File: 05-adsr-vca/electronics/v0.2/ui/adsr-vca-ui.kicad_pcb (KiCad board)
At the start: 2 copper layers, 58 x 110 mm, 31 parts, among them J1 Conn_02x03_Odd_Even, J3 Conn_02x03_Odd_Even, J4 Conn_01x02, J5 Conn_01x06, J6 Conn_02x03_Odd_Even, J8 Conn_02x03_Odd_Even

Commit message: Redraw ADSR PCBs to be on top half of the UI
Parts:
- moved J5 104.5 mm to (143.0, 47.0)
- moved G*** 66.3 mm to (211.4, 50.5)
- moved J3 57.5 mm to (155.5, 91.5), turned to 180 degrees
- moved G*** 56.4 mm to (204.6, 81.1)
- moved J6 45.5 mm to (133.5, 49.5), turned to -90 degrees
- moved D1 17.3 mm to (173.0, 45.7), turned to -90 degrees
- moved J4 16.0 mm to (178.7, 81.6)
- moved H5 13.4 mm to (127.3, 105.7)
- moved H6 13.4 mm to (178.7, 105.7)
- moved J1 7.02 mm to (151.5, 101.0), turned to 90 degrees
- moved J8 6.52 mm to (128.5, 93.5)
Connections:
- J8 pad 2: DECAY_1 -> ATTACK_3
- J8 pad 3: ENV_OUT -> RELEASE_1
- J8 pad 4: ATTACK_3 -> ENV_OUT
- J8 pad 5: unconnected-(J8-Pin_5-Pad5) -> DECAY_1
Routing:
- net VCA_OUT: track 9.75 -> 109.3 mm
- net VCA_IN_DEFAULT: track 19.0 -> 112.5 mm, vias 0 -> 2
- net VCA_CV: track 9.36 -> 88.1 mm
- net VCA_CV_DEFAULT: track 48.0 -> 120.6 mm, vias 2 -> 0
- net SUSTAIN_3: track 104.2 -> 33.9 mm
- net SUSTAIN_1: track 37.0 -> 98.4 mm, vias 0 -> 2
- net SUSTAIN_2: track 37.7 -> 97.7 mm, vias 0 -> 2
- net VCA_OUT_DEFAULT: track 53.9 -> 110.4 mm
- net DECAY_1: track 100.5 -> 65.9 mm, vias 0 -> 1
- net ENV_OUT: track 86.2 -> 59.2 mm, vias 0 -> 2
- net GATE_DEFAULT: track 49.7 -> 73.1 mm, vias 0 -> 4
- net RELEASE_1: track 2.50 -> 19.4 mm, vias 0 -> 1
- net LED_K: track 65.0 -> 48.7 mm, vias 0 -> 2
- net ENV_OUT_DEFAULT: track 65.3 -> 80.4 mm
- net A1_D3_R3: track 65.3 -> 78.9 mm
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
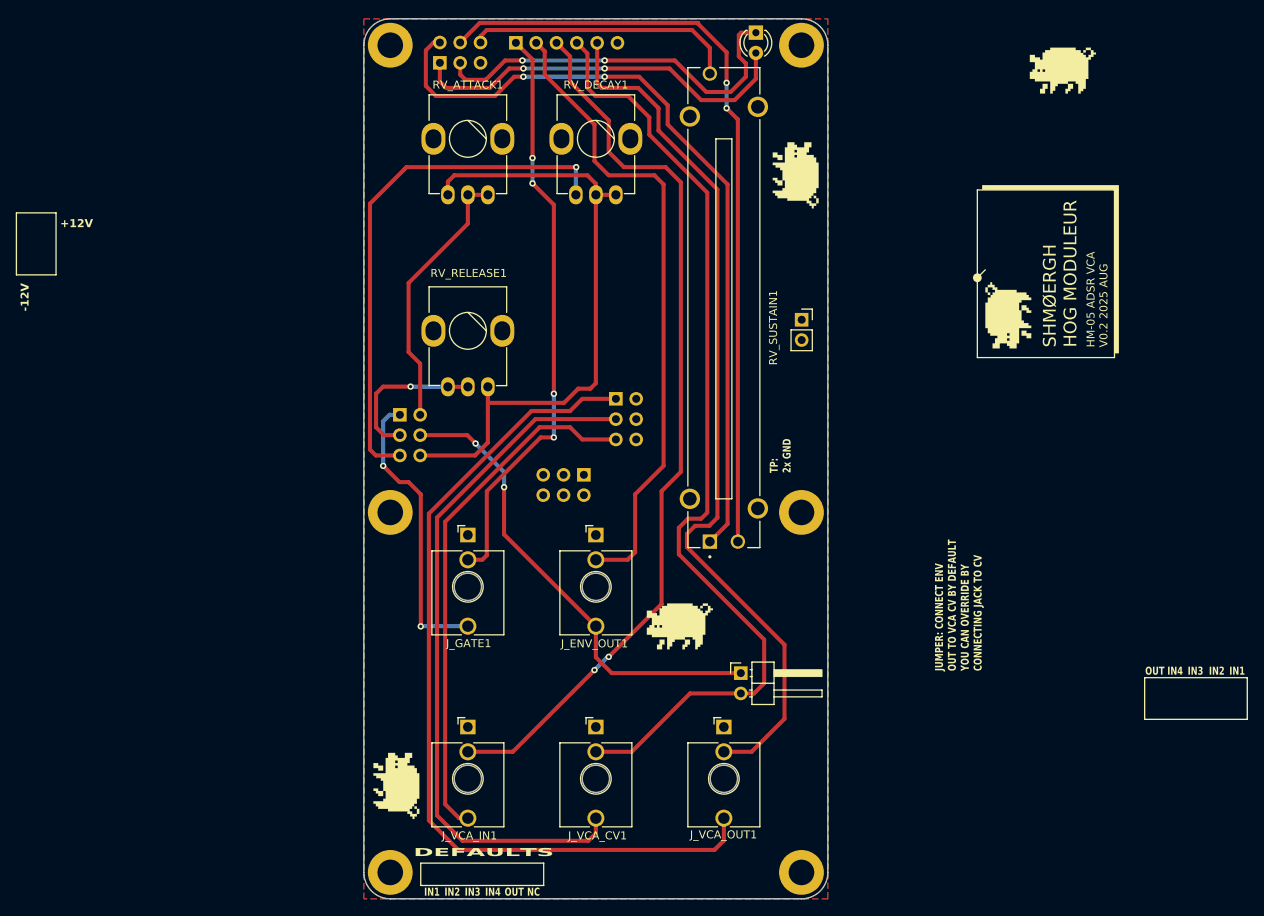
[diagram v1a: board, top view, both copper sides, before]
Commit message: ADSR+VCA UI PCB done
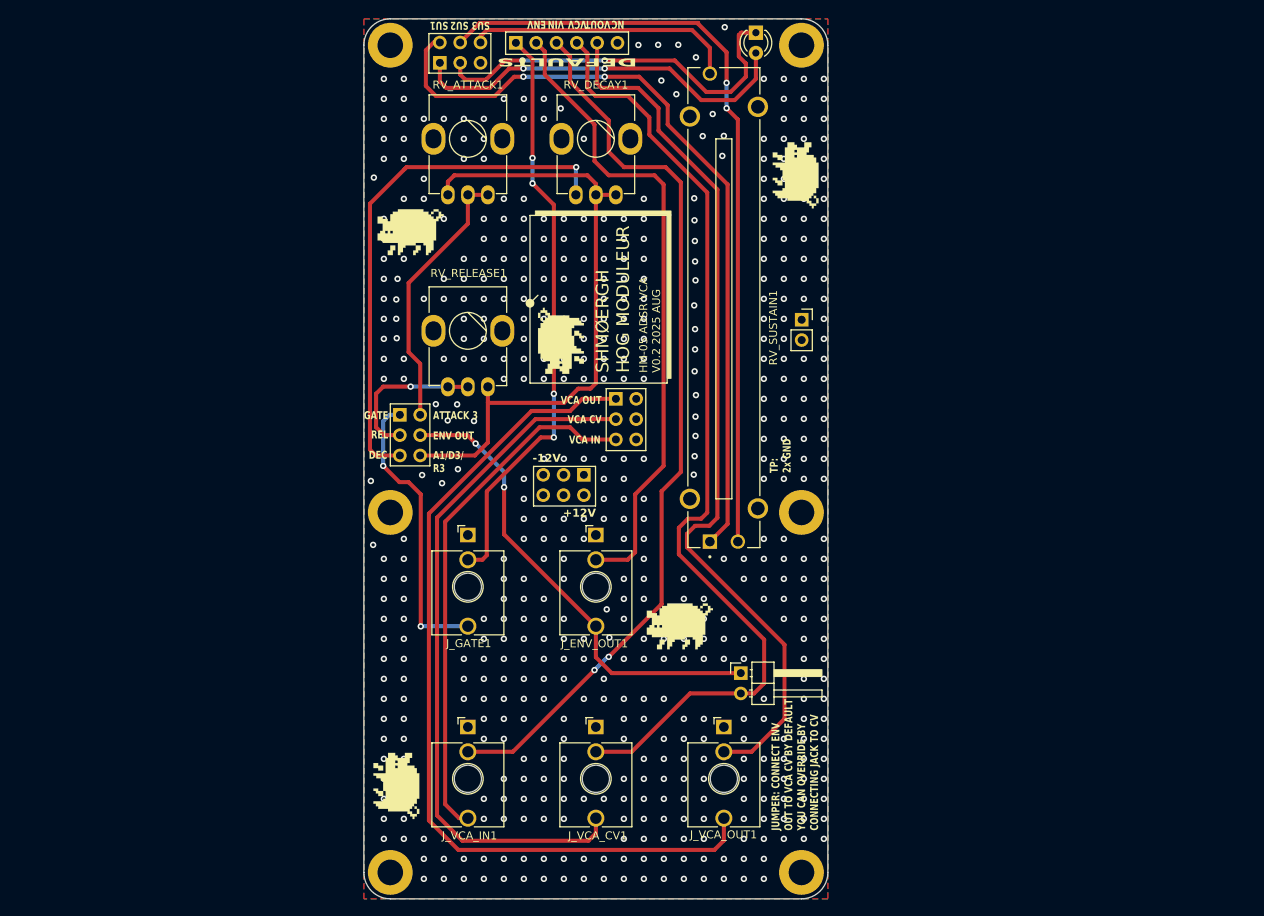
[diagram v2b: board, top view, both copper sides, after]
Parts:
- moved G*** 84.0 mm to (129.8, 70.7)
- moved G*** 56.0 mm to (148.6, 84.3)
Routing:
- net GND: vias 0 -> 542
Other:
- board text added: "A1/D3/ R3"
- board text added: "ATTACK 3"
- board text added: "DEC"
- board text added: "ENV"
- board text added: "ENV OUT"
- board text added: "GATE"
- board text added: "REL"
- board text added: "SU1"
- board text added: "SU2"
- board text added: "SU3"
- board text added: "VCA CV"
- board text added: "VCA IN"
- board text added: "VCA OUT"
- board text added: "VCV"
- board text added: "VIN"
- board text added: "VOUT"
- board text removed: "IN1"
- board text removed: "IN2"
- board text removed: "IN3"
- board text removed: "IN4"
- board text removed: "OUT"
